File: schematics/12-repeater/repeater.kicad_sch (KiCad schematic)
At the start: 11 parts, among them J1 Cat5, J2 PSG01571, U1 PCA9600D

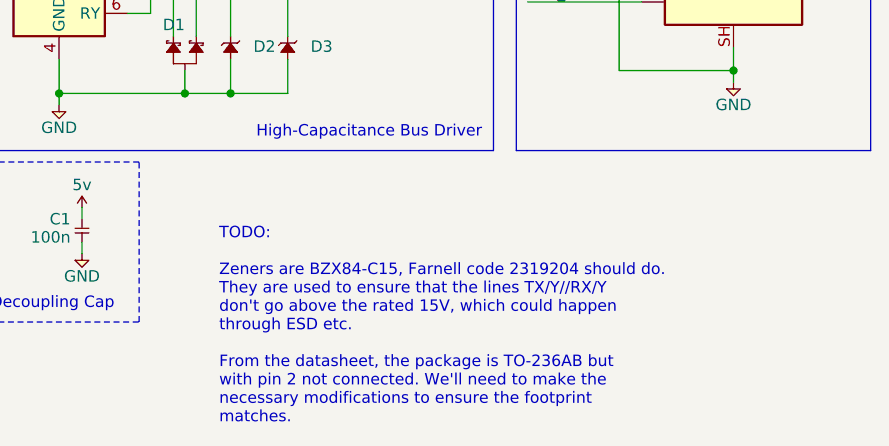
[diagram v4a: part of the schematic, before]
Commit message: added mounting holes
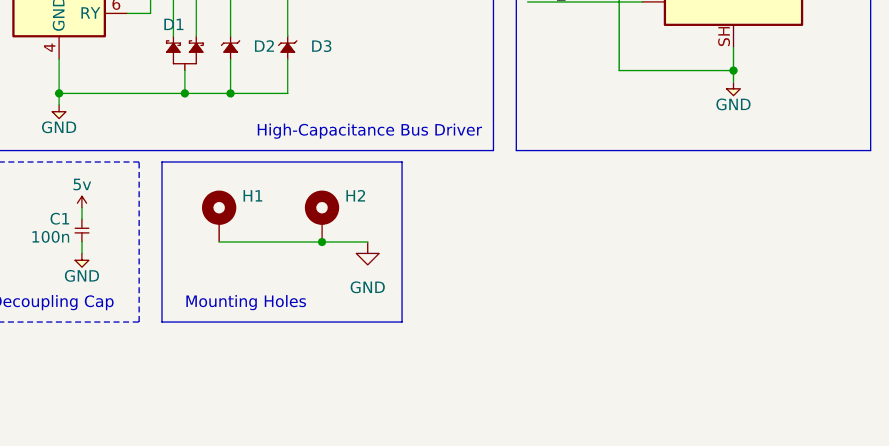
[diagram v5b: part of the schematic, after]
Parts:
- added H1, H2: MountingHole_Pad, royale:MountingHole_Pad, symbol royale:MountingHole_Pad
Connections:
- net GND: now also H1.1, H2.1
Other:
- note added: "Mounting Holes"
- note removed: "TODO: Zeners are BZX84-C15, Farnell code 2319204 should do. They are used to ensure that the lines TX/Y//RX/Y don't go above the rated 15V, which could happen through ESD etc. From the datasheet, the package is TO-236AB but with pin 2 not connected. We'll need to make the necessary modifications to ensure the footprint matches."
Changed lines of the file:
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@@
   (junction (at 158.75 85.09) (diameter 0) (color 0 0 0 0)
+  )
+  (junction (at 160.02 129.54) (diameter 0) (color 0 0 0 0)
   )
   (junction (at 144.78 113.03) (diameter 0) (color 0 0 0 0)
@@
     (stroke (width 0) (type default) (color 0 0 0 0))
   )
+  (wire (pts (xy 160.02 129.54) (xy 165.1 129.54))
+    (stroke (width 0) (type default) (color 0 0 0 0))
+  )
   (polyline (pts (xy 48.26 87.63) (xy 48.26 109.22))
     (stroke (width 0) (type default) (color 0 0 0 0))
@@
     (stroke (width 0) (type default) (color 0 0 0 0))
   )
+  (polyline (pts (xy 142.24 138.43) (xy 168.91 138.43))
+    (stroke (width 0) (type default) (color 0 0 0 0))
+  )
   (polyline (pts (xy 48.26 109.22) (xy 83.82 109.22))
     (stroke (width 0) (type default) (color 0 0 0 0))
@@
     (stroke (width 0) (type default) (color 0 0 0 0))
   )
+  (wire (pts (xy 148.59 129.54) (xy 160.02 129.54))
+    (stroke (width 0) (type default) (color 0 0 0 0))
+  )
   (wire (pts (xy 130.81 109.22) (xy 130.81 113.03))
     (stroke (width 0) (type default) (color 0 0 0 0))
@@
   )
   (polyline (pts (xy 179.07 77.47) (xy 179.07 119.38))
+    (stroke (width 0) (type default) (color 0 0 0 0))
+  )
+  (polyline (pts (xy 142.24 120.65) (xy 168.91 120.65))
     (stroke (width 0) (type default) (color 0 0 0 0))
   )
@@
     (stroke (width 0) (type default) (color 0 0 0 0))
   )
+  (polyline (pts (xy 168.91 138.43) (xy 168.91 120.65))
+    (stroke (width 0) (type default) (color 0 0 0 0))
+  )
   (wire (pts (xy 161.29 91.44) (xy 161.29 101.6))
     (stroke (width 0) (type default) (color 0 0 0 0))
@@
     (stroke (width 0) (type default) (color 0 0 0 0))
   )
+  (polyline (pts (xy 142.24 120.65) (xy 142.24 138.43))
+    (stroke (width 0) (type default) (color 0 0 0 0))
+  )
   (wire (pts (xy 190.5 92.71) (xy 195.58 92.71))
     (stroke (width 0) (type default) (color 0 0 0 0))
@@
     (stroke (width 0) (type default) (color 0 0 0 0))
   )
-  (text "TODO:\n\nZeners are BZX84-C15, Farnell code 2319204 should do.\nThey are used to ensure that the lines TX/Y//RX/Y\ndon't go above the rated 15V, which could happen\nthrough ESD etc.\n\nFrom the datasheet, the package is TO-236AB but\nwith pin 2 not connected. We'll need to make the\nnecessary modifications to ensure the footprint\nmatches."
-    (at 148.59 149.86 0)
-    (effects (font (size 1.27 1.27)) (justify left bottom))
-  )
   (text "Decoupling Cap" (at 123.19 137.16 0)
     (effects (font (size 1.27 1.27)) (justify left bottom))
@@
   (text "Pull-Up Resistors" (at 118.11 118.11 180)
     (effects (font (size 1.27 1.27)) (justify right bottom))
+  )
+  (text "Mounting Holes" (at 144.78 137.16 0)
+    (effects (font (size 1.27 1.27)) (justify left bottom))
   )
   (text "High-Capacitance Bus Driver" (at 177.8 118.11 180)
@@
     )
     (property "Datasheet" "" (id 3) (at 55.88 100.33 0)
+      (effects (font (size 1.27 1.27)) hide)
+    )
+    (pin "1")
+  )
+  (symbol (lib_id "power:GND") (at 165.1 129.54 0) (unit 1)
+    (in_bom yes) (on_board yes) (fields_autoplaced)
+    (property "Reference" "#PWR0101" (id 0) (at 165.1 135.89 0)
+      (effects (font (size 1.27 1.27)) hide)
+    )
+    (property "Value" "GND" (id 1) (at 165.1 134.62 0))
+    (property "Footprint" "" (id 2) (at 165.1 129.54 0)
+      (effects (font (size 1.27 1.27)) hide)
+    )
+    (property "Datasheet" "" (id 3) (at 165.1 129.54 0)
       (effects (font (size 1.27 1.27)) hide)
     )
@@
     (pin "1")
   )
+  (symbol (lib_id "royale:MountingHole_Pad") (at 160.02 127 0) (unit 1)
+    (in_bom yes) (on_board yes)
+    (property "Reference" "H2" (id 0) (at 162.56 124.4599 0)
+      (effects (font (size 1.27 1.27)) (justify left))
+    )
+    (property "Value" "MountingHole_Pad" (id 1) (at 161.29 132.08 0)
+      (effects (font (size 1.27 1.27)) (justify left) hide)
+    )
+    (property "Footprint" "royale:MountingHole_Pad" (id 2) (at 160.02 127 0)
+      (effects (font (size 1.27 1.27)) hide)
+    )
+    (property "Datasheet" "" (id 3) (at 160.02 127 0)
+      (effects (font (size 1.27 1.27)) hide)
+    )
+    (pin "1")
+  )
   (symbol (lib_id "cusf-kicad:GND") (at 133.35 130.81 0) (unit 1)
     (in_bom yes) (on_board yes)
@@
     )
     (property "Datasheet" "" (id 3) (at 133.35 130.81 0)
+      (effects (font (size 1.27 1.27)) hide)
+    )
+    (pin "1")
+  )
+  (symbol (lib_id "royale:MountingHole_Pad") (at 148.59 127 0) (unit 1)
+    (in_bom yes) (on_board yes)
+    (property "Reference" "H1" (id 0) (at 151.13 124.4599 0)
+      (effects (font (size 1.27 1.27)) (justify left))
+    )
+    (property "Value" "MountingHole_Pad" (id 1) (at 142.24 132.08 0)
+      (effects (font (size 1.27 1.27)) (justify left) hide)
+    )
+    (property "Footprint" "royale:MountingHole_Pad" (id 2) (at 148.59 127 0)
+      (effects (font (size 1.27 1.27)) hide)
+    )
+    (property "Datasheet" "" (id 3) (at 148.59 127 0)
       (effects (font (size 1.27 1.27)) hide)
     )
@@
       (reference "#PWR09") (unit 1) (value "GND") (footprint "")
     )
+    (path "/1e1fe0f0-9255-46f7-885e-b30b1e1cfa31"
+      (reference "#PWR0101") (unit 1) (value "GND") (footprint "")
+    )
     (path "/00000000-0000-0000-0000-000061a5eef5"
       (reference "C1") (unit 1) (value "100n") (footprint "Capacitor_SMD:C_0805_2012Metric")
@@
       (reference "D3") (unit 1) (value "Diode_Zener_BZX84-C15") (footprint "Package_TO_SOT_SMD:SOT-23")
     )
+    (path "/d0b8883f-56d3-436a-a178-a658388f963b"
+      (reference "H1") (unit 1) (value "MountingHole_Pad") (footprint "royale:MountingHole_Pad")
+    )
+    (path "/9fa9f26f-181c-4272-9534-03061d2c9314"
+      (reference "H2") (unit 1) (value "MountingHole_Pad") (footprint "royale:MountingHole_Pad")
+    )
     (path "/7188dc85-b662-4454-b487-e52a93f86f4b"

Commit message: Update repeater ready for manufacture
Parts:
- C1: Farnell (none) -> 9406387
- D2, D3: Farnell (none) -> 2319204
- J1: Farnell (none) -> 1849916
- J2: Farnell (none) -> 1280736
- R1, R2: Farnell (none) -> 9333037
- R3, R4: Farnell (none) -> 2447672
- U1: Farnell (none) -> 2775968
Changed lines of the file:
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@@
+      (effects (font (size 1.27 1.27)) hide)
+    )
+    (property "Farnell" "2775968" (id 4) (at 130.81 99.06 0)
       (effects (font (size 1.27 1.27)) hide)
     )
@@
       (effects (font (size 1.27 1.27)) hide)
     )
+    (property "Farnell" "2447672" (id 4) (at 111.76 91.44 0)
+      (effects (font (size 1.27 1.27)) hide)
+    )
     (pin "1")
     (pin "2")
@@
       (effects (font (size 1.27 1.27)) hide)
     )
+    (property "Farnell" "2447672" (id 4) (at 104.14 91.44 0)
+      (effects (font (size 1.27 1.27)) hide)
+    )
     (pin "1")
     (pin "2")
@@
       (effects (font (size 1.27 1.27)) hide)
     )
+    (property "Farnell" "9333037" (id 4) (at 158.75 88.9 0)
+      (effects (font (size 1.27 1.27)) hide)
+    )
     (pin "1")
     (pin "2")
@@
     )
     (property "Datasheet" "" (id 3) (at 161.29 88.9 0)
+      (effects (font (size 1.27 1.27)) hide)
+    )
+    (property "Farnell" "9333037" (id 4) (at 161.29 88.9 0)
       (effects (font (size 1.27 1.27)) hide)
     )
@@
     )
     (property "Datasheet" "" (id 3) (at 133.35 127 0)
+      (effects (font (size 1.27 1.27)) hide)
+    )
+    (property "Farnell" "9406387" (id 4) (at 133.35 127 0)
       (effects (font (size 1.27 1.27)) hide)
     )
@@
       (effects (font (size 1.27 1.27)) hide)
     )
-    (property "Datasheet" "" (id 3) (at 144.78 104.902 0)
+    (property "Datasheet" "https://www.farnell.com/datasheets/2864018.pdf" (id 3) (at 144.78 104.902 0)
       (effects (font (size 1.27 1.27)) hide)
     )
@@
     )
     (property "Datasheet" "" (id 3) (at 156.21 106.68 0)
+      (effects (font (size 1.27 1.27)) hide)
+    )
+    (property "Farnell" "2319204" (id 4) (at 156.21 106.68 0)
       (effects (font (size 1.27 1.27)) hide)
     )
@@
     )
     (property "Datasheet" "~" (id 3) (at 205.74 94.615 90)
+      (effects (font (size 1.27 1.27)) hide)
+    )
+    (property "Farnell" "1849916" (id 4) (at 205.74 95.25 0)
       (effects (font (size 1.27 1.27)) hide)
     )
@@
       (effects (font (size 1.27 1.27)) hide)
     )
-    (property "Datasheet" "" (id 3) (at 149.86 106.68 0)
+    (property "Datasheet" "https://www.farnell.com/datasheets/1808429.pdf" (id 3) (at 149.86 106.68 0)
+      (effects (font (size 1.27 1.27)) hide)
+    )
+    (property "Farnell" "2319204" (id 5) (at 149.86 106.68 0)
       (effects (font (size 1.27 1.27)) hide)
     )
@@
       (effects (font (size 1.27 1.27)) hide)
     )
+    (property "Farnell" "1280736" (id 4) (at 66.04 100.33 0)
+      (effects (font (size 1.27 1.27)) hide)
+    )

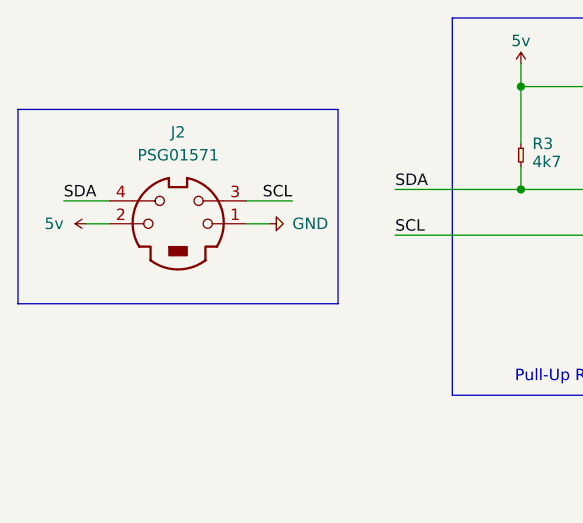
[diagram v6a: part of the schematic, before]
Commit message: Replace mini-DIN with more well-documented part
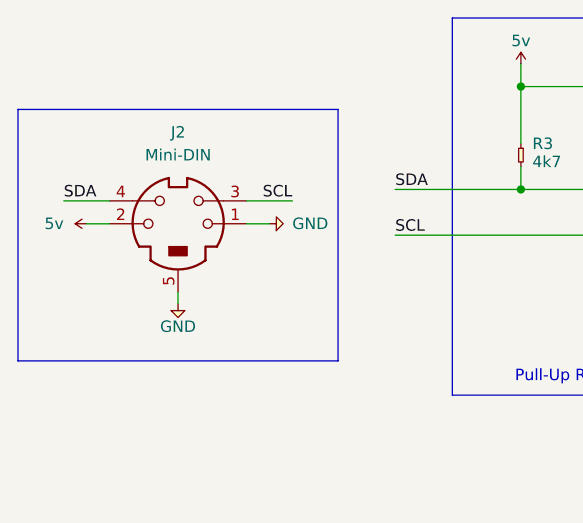
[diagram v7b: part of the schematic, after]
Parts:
- removed J2: PSG01571, royale:Mini-Din-Through-Hole, symbol Connector:Mini-DIN-4
- added J2: Mini-DIN, royale:TE_5749181-1, symbol royale:Mini-DIN-4-Shielded
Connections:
- net 1v8: now also J2.2
- net GND: now also J2.1, J2.5
- net SCL: now also J2.3
- net SDA: now also J2.4
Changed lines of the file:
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@@
     (stroke (width 0) (type default) (color 0 0 0 0))
   )
-  (polyline (pts (xy 48.26 87.63) (xy 48.26 109.22))
+  (polyline (pts (xy 48.26 87.63) (xy 48.26 115.57))
     (stroke (width 0) (type default) (color 0 0 0 0))
   )
@@
     (stroke (width 0) (type default) (color 0 0 0 0))
   )
-  (polyline (pts (xy 48.26 109.22) (xy 83.82 109.22))
+  (polyline (pts (xy 48.26 115.57) (xy 83.82 115.57))
     (stroke (width 0) (type default) (color 0 0 0 0))
   )
@@
   )
   (wire (pts (xy 111.76 101.6) (xy 123.19 101.6))
+    (stroke (width 0) (type default) (color 0 0 0 0))
+  )
+  (wire (pts (xy 66.04 107.95) (xy 66.04 109.22))
     (stroke (width 0) (type default) (color 0 0 0 0))
   )
@@
     (stroke (width 0) (type default) (color 0 0 0 0))
   )
-  (polyline (pts (xy 83.82 109.22) (xy 83.82 87.63))
+  (polyline (pts (xy 83.82 115.57) (xy 83.82 87.63))
     (stroke (width 0) (type default) (color 0 0 0 0))
   )
@@
   (symbol (lib_id "cusf-kicad:GND") (at 130.81 114.3 0) (unit 1)
     (in_bom yes) (on_board yes)
-    (property "Reference" "#PWR07" (id 0) (at 127.508 113.284 0)
+    (property "Reference" "#PWR08" (id 0) (at 127.508 113.284 0)
       (effects (font (size 1.27 1.27)) (justify left) hide)
     )
@@
   (symbol (lib_id "power:GND") (at 165.1 129.54 0) (unit 1)
     (in_bom yes) (on_board yes) (fields_autoplaced)
-    (property "Reference" "#PWR0101" (id 0) (at 165.1 135.89 0)
+    (property "Reference" "#PWR010" (id 0) (at 165.1 135.89 0)
       (effects (font (size 1.27 1.27)) hide)
     )
@@
   (symbol (lib_id "cusf-kicad:GND") (at 205.74 111.76 0) (unit 1)
     (in_bom yes) (on_board yes)
-    (property "Reference" "#PWR06" (id 0) (at 202.438 110.744 0)
+    (property "Reference" "#PWR07" (id 0) (at 202.438 110.744 0)
       (effects (font (size 1.27 1.27)) (justify left) hide)
     )
@@
     (pin "3")
   )
-  (symbol (lib_id "Connector:Mini-DIN-4") (at 66.04 100.33 0) (unit 1)
-    (in_bom yes) (on_board yes)
-    (property "Reference" "J2" (id 0) (at 66.04 90.17 0))
-    (property "Value" "PSG01571" (id 1) (at 66.0577 92.71 0))
-    (property "Footprint" "royale:Mini-Din-Through-Hole" (id 2) (at 66.04 100.33 0)
+  (symbol (lib_id "royale:Mini-DIN-4-Shielded") (at 66.04 100.33 0) (unit 1)
+    (in_bom yes) (on_board yes) (fields_autoplaced)
+    (property "Reference" "J2" (id 0) (at 66.0577 90.17 0))
+    (property "Value" "Mini-DIN" (id 1) (at 66.0577 92.71 0))
+    (property "Footprint" "royale:TE_5749181-1" (id 2) (at 66.04 100.33 0)
       (effects (font (size 1.27 1.27)) hide)
     )
@@
       (effects (font (size 1.27 1.27)) hide)
     )
-    (property "Farnell" "1280736" (id 4) (at 66.04 100.33 0)
+    (property "Farnell" "3791398" (id 4) (at 66.04 100.33 0)
       (effects (font (size 1.27 1.27)) hide)
     )
@@
     (pin "3")
     (pin "4")
+    (pin "5")
   )
   (symbol (lib_id "royale:5v") (at 190.5 82.55 0) (unit 1)
@@
   (symbol (lib_id "cusf-kicad:GND") (at 133.35 130.81 0) (unit 1)
     (in_bom yes) (on_board yes)
-    (property "Reference" "#PWR09" (id 0) (at 130.048 129.794 0)
+    (property "Reference" "#PWR011" (id 0) (at 130.048 129.794 0)
       (effects (font (size 1.27 1.27)) (justify left) hide)
     )
@@
     (pin "1")
   )
+  (symbol (lib_id "cusf-kicad:GND") (at 66.04 109.22 0) (unit 1)
+    (in_bom yes) (on_board yes)
+    (property "Reference" "#PWR06" (id 0) (at 62.738 108.204 0)
+      (effects (font (size 1.27 1.27)) (justify left) hide)
+    )
+    (property "Value" "GND" (id 1) (at 66.04 111.76 0))
+    (property "Footprint" "" (id 2) (at 66.04 109.22 0)
+      (effects (font (size 1.27 1.27)) hide)
+    )
+    (property "Datasheet" "" (id 3) (at 66.04 109.22 0)
+      (effects (font (size 1.27 1.27)) hide)
+    )
+    (pin "1")
+  )
   (symbol (lib_id "royale:MountingHole_Pad") (at 148.59 127 0) (unit 1)
     (in_bom yes) (on_board yes)
@@
   (symbol (lib_id "royale:5v") (at 133.35 125.73 0) (unit 1)
     (in_bom yes) (on_board yes)
-    (property "Reference" "#PWR08" (id 0) (at 133.35 122.936 0)
+    (property "Reference" "#PWR09" (id 0) (at 133.35 122.936 0)
       (effects (font (size 1.27 1.27)) (justify left) hide)
     )
@@
       (reference "#PWR05") (unit 1) (value "GND") (footprint "")
     )
+    (path "/c6906766-56fa-4c03-8c3f-038f5d19d9a5"
+      (reference "#PWR06") (unit 1) (value "GND") (footprint "")
+    )
     (path "/4a81e688-46c9-4478-a887-1fe0572879c7"
-      (reference "#PWR06") (unit 1) (value "GND") (footprint "")
+      (reference "#PWR07") (unit 1) (value "GND") (footprint "")
     )
     (path "/00000000-0000-0000-0000-000061a2a4f9"
-      (reference "#PWR07") (unit 1) (value "GND") (footprint "")
+      (reference "#PWR08") (unit 1) (value "GND") (footprint "")
     )
     (path "/f37200eb-4ba2-469b-8c3b-abb7a306b603"
-      (reference "#PWR08") (unit 1) (value "5v") (footprint "")
+      (reference "#PWR09") (unit 1) (value "5v") (footprint "")
+    )
+    (path "/1e1fe0f0-9255-46f7-885e-b30b1e1cfa31"
+      (reference "#PWR010") (unit 1) (value "GND") (footprint "")
     )
     (path "/a24443c3-b0da-460b-a1bd-69c4956ceecf"
-      (reference "#PWR09") (unit 1) (value "GND") (footprint "")
-    )
-    (path "/1e1fe0f0-9255-46f7-885e-b30b1e1cfa31"
-      (reference "#PWR0101") (unit 1) (value "GND") (footprint "")
+      (reference "#PWR011") (unit 1) (value "GND") (footprint "")
     )
     (path "/00000000-0000-0000-0000-000061a5eef5"
@@
       (reference "J1") (unit 1) (value "Cat5") (footprint "royale:RJ45_Amphenol_RJHSE5380")
     )
-    (path "/91b1515f-01d7-467f-9976-fa4a3565e617"
-      (reference "J2") (unit 1) (value "PSG01571") (footprint "royale:Mini-Din-Through-Hole")
+    (path "/913c3521-e6c4-4f5d-aba0-0a041247ed6a"
+      (reference "J2") (unit 1) (value "Mini-DIN") (footprint "royale:TE_5749181-1")
     )
     (path "/00000000-0000-0000-0000-000061a1c730"

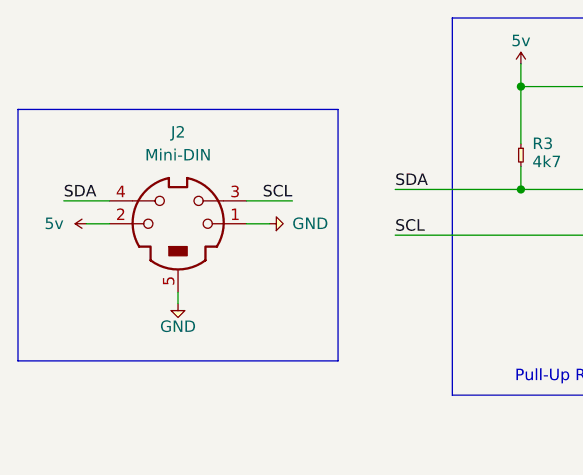
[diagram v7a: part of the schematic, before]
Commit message: Minor cleanup to accomodate new connector
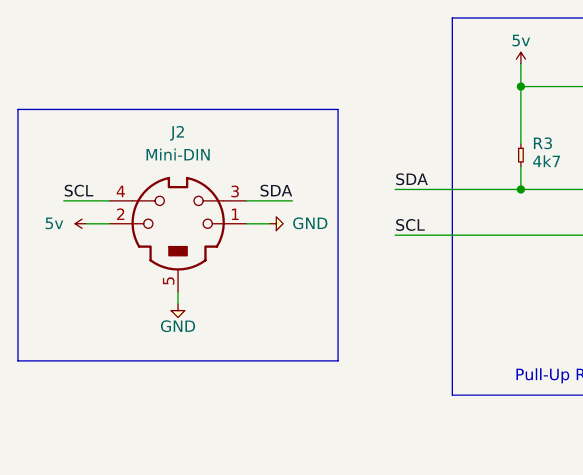
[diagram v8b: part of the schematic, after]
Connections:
- net SCL: now also J2.4; no longer J2.3
- net SDA: now also J2.3; no longer J2.4
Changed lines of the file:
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@@
     (effects (font (size 1.27 1.27)) (justify right bottom))
   )
-  (label "SCL" (at 78.74 97.79 180)
-    (effects (font (size 1.27 1.27)) (justify right bottom))
+  (label "SCL" (at 53.34 97.79 0)
+    (effects (font (size 1.27 1.27)) (justify left bottom))
   )
   (label "SCL_D" (at 176.53 101.6 180)
@@
     (effects (font (size 1.27 1.27)) (justify left bottom))
   )
-  (label "SDA" (at 53.34 97.79 0)
-    (effects (font (size 1.27 1.27)) (justify left bottom))
+  (label "SDA" (at 78.74 97.79 180)
+    (effects (font (size 1.27 1.27)) (justify right bottom))
   )
   (label "SCL" (at 90.17 101.6 0)
